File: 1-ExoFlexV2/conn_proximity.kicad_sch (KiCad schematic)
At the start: 44 parts, among them J35 2, J36 2, J37 2, J38 2, J39 4, J40 4, J41 4, J42 4, J43 Jumper, J44 Jumper, J45 Jumper, J46 Jumper

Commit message: PLACEMENT 1
- Placement des connnecteurs
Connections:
- net +5VA is gone; now on net +5V: J43.1 (Pin_1), J44.1 (Pin_1), J45.1 (Pin_1), J46.1 (Pin_1)
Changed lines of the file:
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@@
     (pin "04")
-  )
-  (symbol (lib_id "power:+5VA") (at 184.15 60.96 0) (unit 1)
-    (in_bom yes) (on_board yes) (fields_autoplaced)
-    (property "Reference" "#PWR0104" (id 0) (at 184.15 64.77 0)
-      (effects (font (size 1.27 1.27)) hide)
-    )
-    (property "Value" "+5VA" (id 1) (at 184.15 55.88 0))
-    (property "Footprint" "" (id 2) (at 184.15 60.96 0)
-      (effects (font (size 1.27 1.27)) hide)
-    )
-    (property "Datasheet" "" (id 3) (at 184.15 60.96 0)
-      (effects (font (size 1.27 1.27)) hide)
-    )
-    (pin "1")
   )
   (symbol (lib_id "Device:D_Zener") (at 43.18 113.03 270) (unit 1)
@@
     (pin "02")
   )
+  (symbol (lib_id "power:+5V") (at 185.42 100.33 0) (unit 1)
+    (in_bom yes) (on_board yes) (fields_autoplaced)
+    (property "Reference" "#PWR0105" (id 0) (at 185.42 104.14 0)
+      (effects (font (size 1.27 1.27)) hide)
+    )
+    (property "Value" "+5V" (id 1) (at 185.42 95.25 0))
+    (property "Footprint" "" (id 2) (at 185.42 100.33 0)
+      (effects (font (size 1.27 1.27)) hide)
+    )
+    (property "Datasheet" "" (id 3) (at 185.42 100.33 0)
+      (effects (font (size 1.27 1.27)) hide)
+    )
+    (pin "1")
+  )
   (symbol (lib_id "power:GND") (at 30.48 41.91 0) (unit 1)
     (in_bom yes) (on_board yes) (fields_autoplaced)
@@
     (pin "1")
     (pin "2")
-  )
-  (symbol (lib_id "power:+5VA") (at 184.15 20.32 0) (unit 1)
-    (in_bom yes) (on_board yes) (fields_autoplaced)
-    (property "Reference" "#PWR0103" (id 0) (at 184.15 24.13 0)
-      (effects (font (size 1.27 1.27)) hide)
-    )
-    (property "Value" "+5VA" (id 1) (at 184.15 15.24 0))
-    (property "Footprint" "" (id 2) (at 184.15 20.32 0)
-      (effects (font (size 1.27 1.27)) hide)
-    )
-    (property "Datasheet" "" (id 3) (at 184.15 20.32 0)
-      (effects (font (size 1.27 1.27)) hide)
-    )
-    (pin "1")
   )
   (symbol (lib_id "Device:R_Small_US") (at 50.8 30.48 90) (unit 1)
@@
     (pin "3")
   )
+  (symbol (lib_id "power:+5V") (at 184.15 60.96 0) (unit 1)
+    (in_bom yes) (on_board yes) (fields_autoplaced)
+    (property "Reference" "#PWR0104" (id 0) (at 184.15 64.77 0)
+      (effects (font (size 1.27 1.27)) hide)
+    )
+    (property "Value" "+5V" (id 1) (at 184.15 55.88 0))
+    (property "Footprint" "" (id 2) (at 184.15 60.96 0)
+      (effects (font (size 1.27 1.27)) hide)
+    )
+    (property "Datasheet" "" (id 3) (at 184.15 60.96 0)
+      (effects (font (size 1.27 1.27)) hide)
+    )
+    (pin "1")
+  )
   (symbol (lib_id "power:GND") (at 101.6 173.99 0) (unit 1)
     (in_bom yes) (on_board yes) (fields_autoplaced)
@@
     (pin "2")
   )
-  (symbol (lib_id "power:+5VA") (at 185.42 100.33 0) (unit 1)
-    (in_bom yes) (on_board yes) (fields_autoplaced)
-    (property "Reference" "#PWR0105" (id 0) (at 185.42 104.14 0)
-      (effects (font (size 1.27 1.27)) hide)
-    )
-    (property "Value" "+5VA" (id 1) (at 185.42 95.25 0))
-    (property "Footprint" "" (id 2) (at 185.42 100.33 0)
-      (effects (font (size 1.27 1.27)) hide)
-    )
-    (property "Datasheet" "" (id 3) (at 185.42 100.33 0)
-      (effects (font (size 1.27 1.27)) hide)
-    )
-    (pin "1")
-  )
   (symbol (lib_id "Device:D_Zener") (at 36.83 113.03 270) (unit 1)
     (in_bom yes) (on_board yes)
@@
     (pin "1")
     (pin "2")
+  )
+  (symbol (lib_id "power:+5V") (at 185.42 140.97 0) (unit 1)
+    (in_bom yes) (on_board yes) (fields_autoplaced)
+    (property "Reference" "#PWR0106" (id 0) (at 185.42 144.78 0)
+      (effects (font (size 1.27 1.27)) hide)
+    )
+    (property "Value" "+5V" (id 1) (at 185.42 135.89 0))
+    (property "Footprint" "" (id 2) (at 185.42 140.97 0)
+      (effects (font (size 1.27 1.27)) hide)
+    )
+    (property "Datasheet" "" (id 3) (at 185.42 140.97 0)
+      (effects (font (size 1.27 1.27)) hide)
+    )
+    (pin "1")
   )
   (symbol (lib_id "power:GND") (at 30.48 116.84 0) (unit 1)
@@
     (pin "2")
     (pin "3")
+  )
+  (symbol (lib_id "power:+5V") (at 184.15 20.32 0) (unit 1)
+    (in_bom yes) (on_board yes) (fields_autoplaced)
+    (property "Reference" "#PWR0103" (id 0) (at 184.15 24.13 0)
+      (effects (font (size 1.27 1.27)) hide)
+    )
+    (property "Value" "+5V" (id 1) (at 184.15 15.24 0))
+    (property "Footprint" "" (id 2) (at 184.15 20.32 0)
+      (effects (font (size 1.27 1.27)) hide)
+    )
+    (property "Datasheet" "" (id 3) (at 184.15 20.32 0)
+      (effects (font (size 1.27 1.27)) hide)
+    )
+    (pin "1")
   )
   (symbol (lib_id "Connector:Conn_01x03_Male") (at 176.53 110.49 0) (mirror y) (unit 1)
@@
     (pin "02")
   )
-  (symbol (lib_id "power:+5VA") (at 185.42 140.97 0) (unit 1)
-    (in_bom yes) (on_board yes) (fields_autoplaced)
-    (property "Reference" "#PWR0106" (id 0) (at 185.42 144.78 0)
-      (effects (font (size 1.27 1.27)) hide)
-    )
-    (property "Value" "+5VA" (id 1) (at 185.42 135.89 0))
-    (property "Footprint" "" (id 2) (at 185.42 140.97 0)
-      (effects (font (size 1.27 1.27)) hide)
-    )
-    (property "Datasheet" "" (id 3) (at 185.42 140.97 0)
-      (effects (font (size 1.27 1.27)) hide)
-    )
-    (pin "1")
-  )
   (symbol (lib_id "power:+5V") (at 53.34 63.5 0) (unit 1)

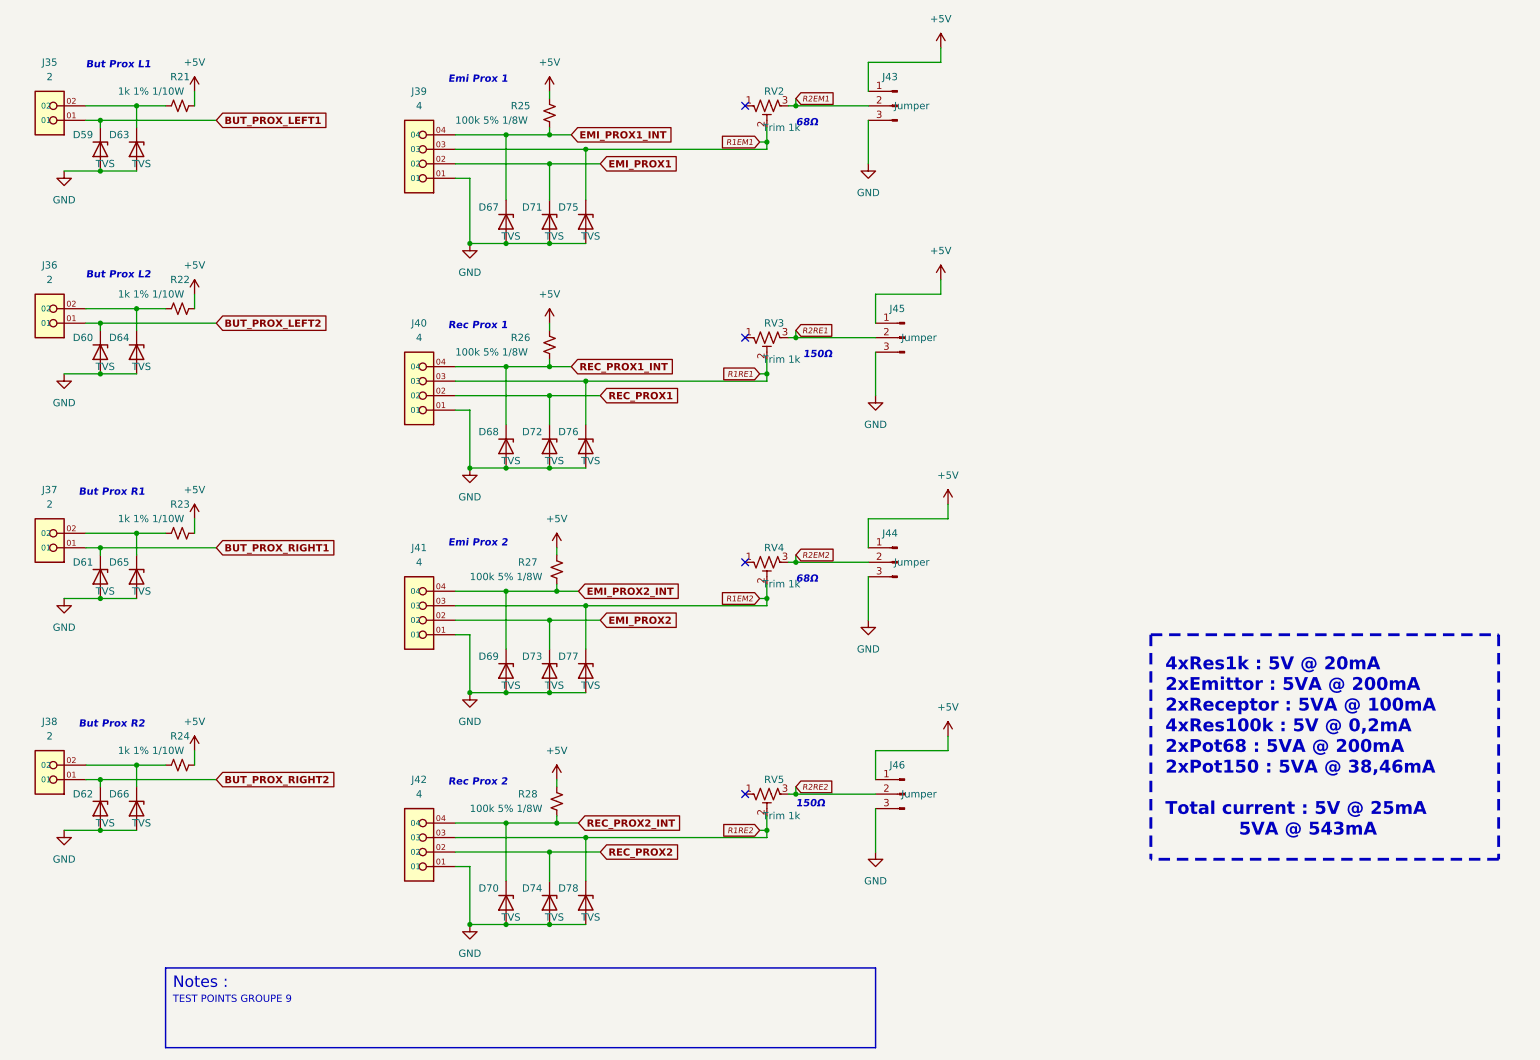
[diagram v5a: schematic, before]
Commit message: Finalisation 3
- Changement des régulateur de tension
- Retrait de test point inutile
- Changement de jumper mal positionner
- Ajout de Mounting holes et fiducial
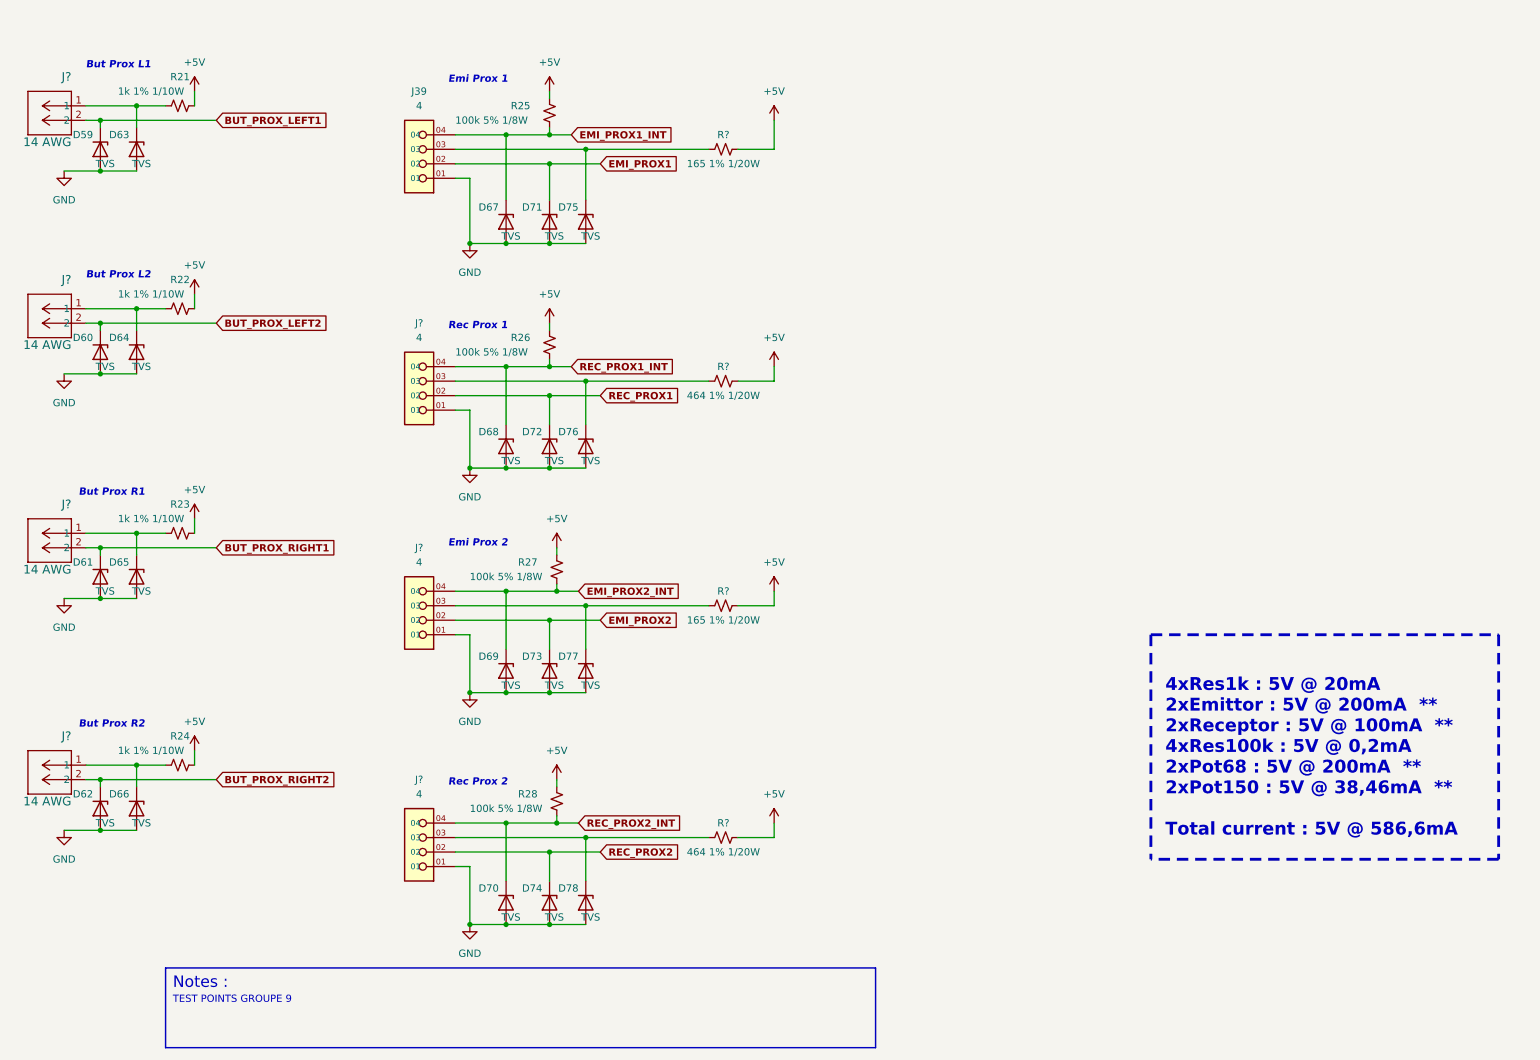
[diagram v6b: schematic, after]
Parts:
- removed J35, J36, J37, J38: 2, FootPrint:PHOENIX_1751099, symbol SymLib:1751099
- removed J40, J41, J42: 4, FootPrint:PHOENIX_1751112, symbol SymLib:1751112
- removed J43, J44, J45, J46: Jumper, Connector_PinSocket_2.54mm:PinSocket_1x03_P2.54mm_Vertical, symbol Connector:Conn_01x03_Male
- removed RV2, RV3, RV4, RV5: Trim 1k, FootPrint:TRIM_3362P-1-102LF, symbol Device:R_Potentiometer_Trim_US
- added J? (x3): 4, FootPrint:PHOENIX_1755752, symbol SymLib:1751112
- added J? (x4): 14 AWG, FootPrintLib:PHOENIX_1755736, symbol SymLib:1729128
- added R? (x2): 165 1% 1/20W, Resistor_SMD:R_0201_0603Metric, symbol Device:R_Small_US
- added R? (x2): 464 1% 1/20W, Resistor_SMD:R_0201_0603Metric, symbol Device:R_Small_US
- J39: footprint FootPrint:PHOENIX_1751112 -> FootPrint:PHOENIX_1755752; DESCRIPTION 4 Position Wire to Board Terminal Block 55° (125°) Angle wi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 -> 4 Position Terminal Block Header, Male Pins, Shrouded (4 Si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; PACKAGE 4 POS 0.100" (2.54mm) -> 4 POS 0.200" (5.08mm); PART NUMBER 1751112 -> 1755752
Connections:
- net +5V: now also R?.1, R?.1, R?.1, R?.1
- net BUT_PROX_LEFT1: now also J?.2
- net BUT_PROX_LEFT2: now also J?.2
- net BUT_PROX_RIGHT1: now also J?.2
- net BUT_PROX_RIGHT2: now also J?.2
- net EMI_PROX2: now also J?.02
- net EMI_PROX2_INT: now also J?.04
- net GND: now also J?.01, J?.01, J?.01
- net REC_PROX1: now also J?.02
- net REC_PROX1_INT: now also J?.04
- net REC_PROX2: now also J?.02
- net REC_PROX2_INT: now also J?.04
- net at D65.1 (K), R23.1: now also J?.1
- net at D64.1 (K), R22.1: now also J?.1
- net at D66.1 (K), R24.1: now also J?.1
- net at D63.1 (K), R21.1: now also J?.1
- net R1EM1: no longer names the net of D75.1 (K), J39.03
- net R1EM1: now also R?.2
- net R1EM2: no longer names the net of D77.1 (K)
- net R1EM2: now also J?.03, R?.2
- net R1RE1: no longer names the net of D76.1 (K)
- net R1RE1: now also J?.03, R?.2
- net R1RE2: no longer names the net of D78.1 (K)
- net R1RE2: now also J?.03, R?.2
- no-connect marks 4 -> 0
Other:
- note added: "4xRes1k : 5V @ 20mA 2xEmittor : 5V @ 200mA ** 2xReceptor : 5V @ 100mA ** 4xRes100k : 5V @ 0,2mA 2xPot68 : 5V @ 200mA ** 2xPot150 : 5V @ 38,46mA ** Total current : 5V @ 586,6mA"
- note removed: "150Ω"
- note removed: "4xRes1k : 5V @ 20mA 2xEmittor : 5VA @ 200mA 2xReceptor : 5VA @ 100mA 4xRes100k : 5V @ 0,2mA 2xPot68 : 5VA @ 200mA 2xPot150 : 5VA @ 38,46mA Total current : 5V @ 25mA 5VA @ 543mA"
- note removed: "68Ω"

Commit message: Finalisation schéma FIN
- Changement des uméro pour les inverseurs
- Changement des connecteur et début de placement
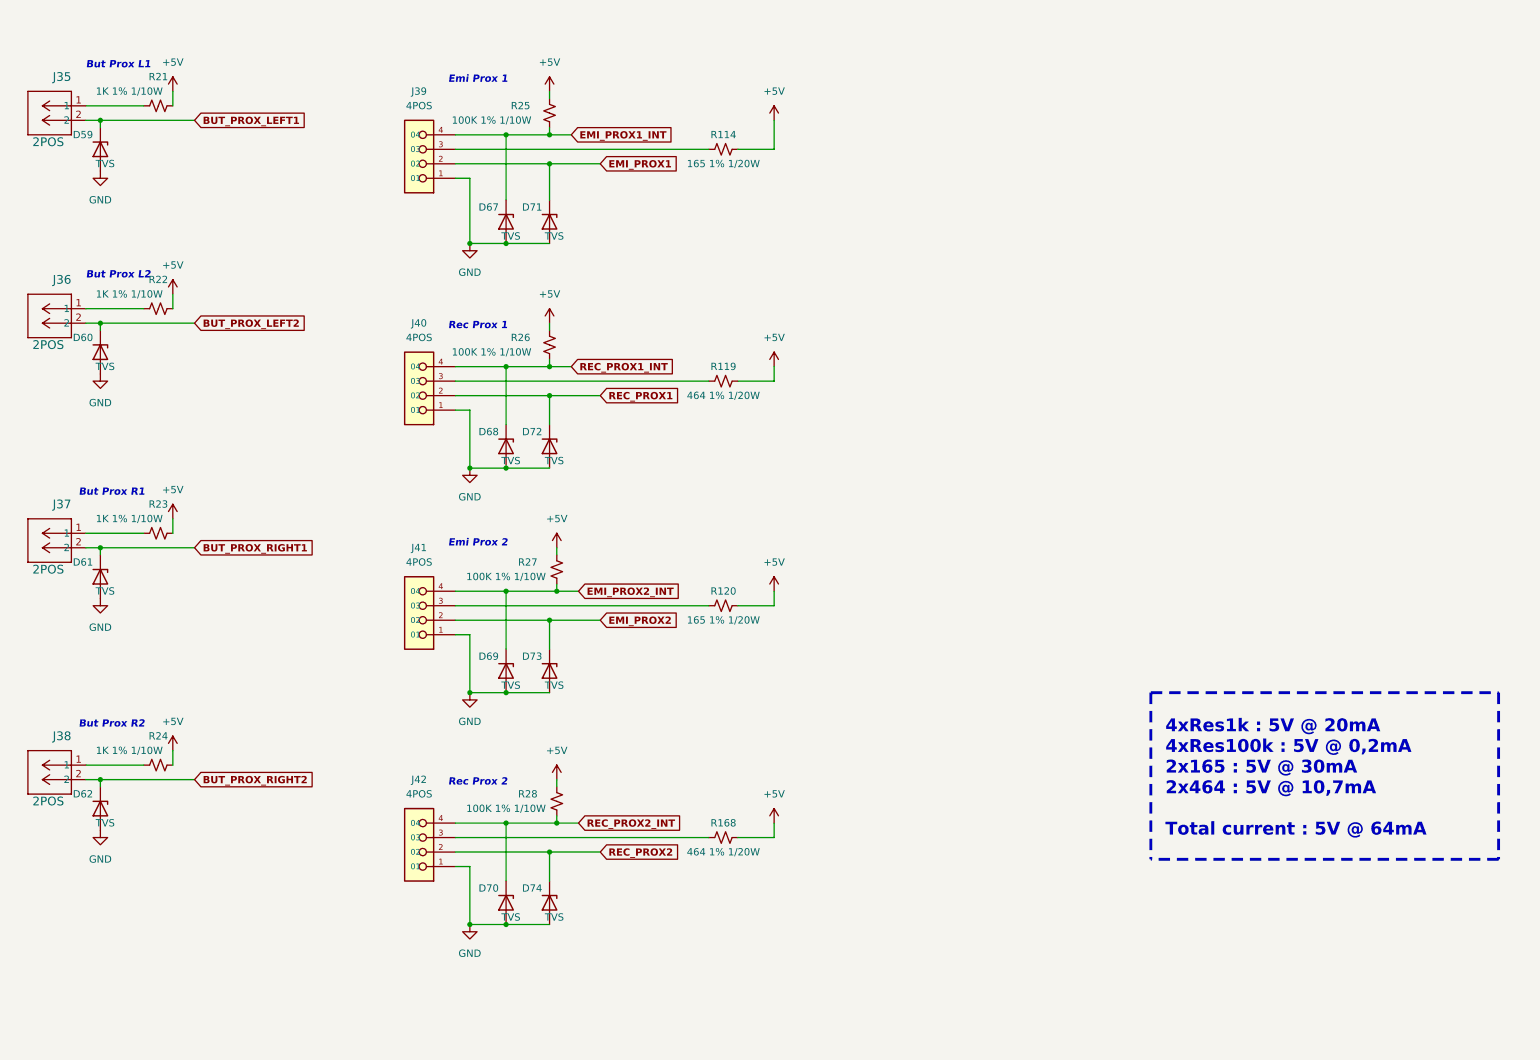
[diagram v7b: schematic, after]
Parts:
- removed D63, D64, D65, D66, D75, D76, D77, D78: TVS, FootPrint:DPY2_TEX, symbol Device:D_Zener
- removed J? (x4): 14 AWG, FootPrintLib:PHOENIX_1755736, symbol SymLib:1729128
- added J35, J36, J37, J38: 2POS, FootPrintLib:CON_39281023, symbol SymLib:1729128
- J39: value 4 -> 4POS; footprint FootPrint:PHOENIX_1755752 -> FootPrint:CON_39301049; DESCRIPTION 4 Position Terminal Block Header, Male Pins, Shrouded (4 Si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 -> Connector Header Through Hole 4 position 0.165" (4.20mm); MANUFACTURER Phoenix Contact -> Molex; PACKAGE 4 POS 0.200" (5.08mm) -> 4 POS 0.165" (4,2mm); PART NUMBER 1755752 -> 0039301049
- J40, J41, J42: renamed from J?; value 4 -> 4POS; footprint FootPrint:PHOENIX_1755752 -> FootPrint:CON_39301049; DESCRIPTION 4 Position Terminal Block Header, Male Pins, Shrouded (4 Si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 -> Connector Header Through Hole 4 position 0.165" (4.20mm); MANUFACTURER Phoenix Contact -> Molex; PACKAGE 4 POS 0.200" (5.08mm) -> 4 POS 0.165" (4,2mm); PART NUMBER 1755752 -> 0039301049
- R21, R22, R23, R24: value 1k 1% 1/10W -> 1K 1% 1/10W; footprint Resistor_SMD:R_0402_1005Metric -> Resistor_SMD:R_0603_1608Metric; DESCRIPTION 1 kOhms ±1% 0.1W, 1/10W Chip Resistor 0402 (1005 Metric) Au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 -> 1 kOhms ±1% 0.1W, 1/10W Chip Resistor 0603 (1608 Metric) Au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; PACKAGE 0402 (1005 Metric) -> 0603 (1608 Metric); PART NUMBER ERJ-2RKF1001X -> ERJ-3EKF1001V
- R25, R26, R27, R28: value 100k 5% 1/8W -> 100K 1% 1/10W; footprint Resistor_SMD:R_0805_2012Metric -> Resistor_SMD:R_0603_1608Metric; DESCRIPTION 100 kOhms ±5% 0.125W, 1/8W Chip Resistor 0805 (2012 Metric)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 -> 100 kOhms ±1% 0.1W, 1/10W Chip Resistor 0603 (1608 Metric) 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; PACKAGE 0805 (2012 Metric) -> 0603 (1608 Metric); PART NUMBER ERJ-6GEYJ104V -> ERJ-3EKF1003V
- gave numbers to parts that had none: 4
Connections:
- net BUT_PROX_LEFT1: now also J35.2
- net BUT_PROX_LEFT2: now also J36.2
- net BUT_PROX_RIGHT1: now also J37.2
- net BUT_PROX_RIGHT2: now also J38.2
- net EMI_PROX1: now also J39.2 (02); no longer J39.02
- net EMI_PROX1_INT: now also J39.4 (04); no longer J39.04
- net EMI_PROX2: now also J41.2 (02); no longer J41.02
- net EMI_PROX2_INT: now also J41.4 (04); no longer J41.04
- net GND: now also J39.1 (01), J40.1 (01), J41.1 (01), J42.1 (01); no longer J39.01, J40.01, J41.01, J42.01
- net REC_PROX1: now also J40.2 (02); no longer J40.02
- net REC_PROX1_INT: now also J40.4 (04); no longer J40.04
- net REC_PROX2: now also J42.2 (02); no longer J42.02
- net REC_PROX2_INT: now also J42.4 (04); no longer J42.04
- net at R119.2: now also J40.3 (03); no longer J40.03
- net at R22.1: now also J36.1
- net at R24.1: now also J38.1
- net at R23.1: now also J37.1
- net at R120.2: now also J41.3 (03); no longer J41.03
- net at R168.2: now also J42.3 (03); no longer J42.03
- net at R21.1: now also J35.1
- net at R114.2: now also J39.3 (03); no longer J39.03
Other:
- note added: "4xRes1k : 5V @ 20mA 4xRes100k : 5V @ 0,2mA 2x165 : 5V @ 30mA 2x464 : 5V @ 10,7mA Total current : 5V @ 64mA"
- note removed: "4xRes1k : 5V @ 20mA 2xEmittor : 5V @ 200mA ** 2xReceptor : 5V @ 100mA ** 4xRes100k : 5V @ 0,2mA 2xPot68 : 5V @ 200mA ** 2xPot150 : 5V @ 38,46mA ** Total current : 5V @ 586,6mA"
- note removed: "Notes :"
- note removed: "TEST POINTS GROUPE 9"
- moved on the sheet: R21, R22, R23, R24
